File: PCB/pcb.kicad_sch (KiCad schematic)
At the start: 19 parts, among them J2 Conn_01x04, Q1 2N7002, SW1 SW_Push, U1 AT90USB1286-AU, Y1 Crystal_GND24_Small

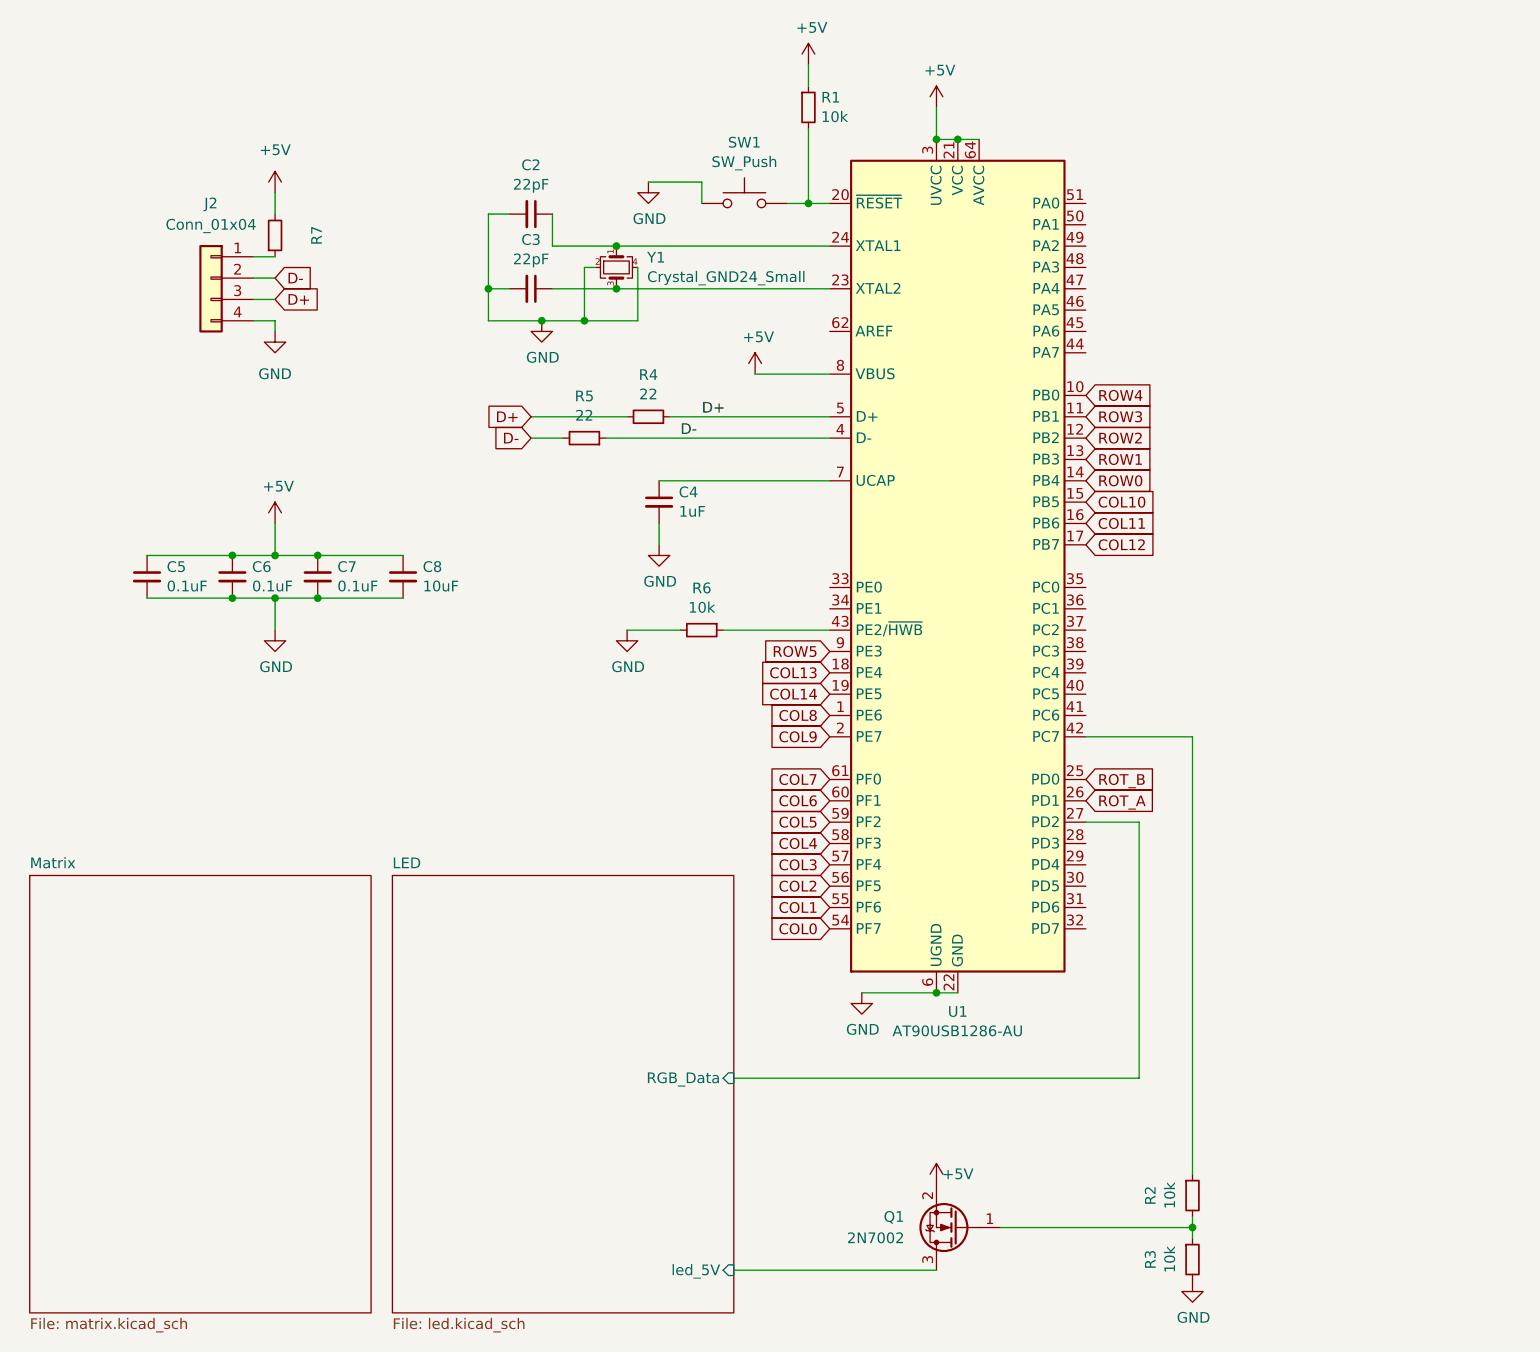
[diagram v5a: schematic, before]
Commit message: changes:\n\n -change zones\n -add mounting holes\n -change via size
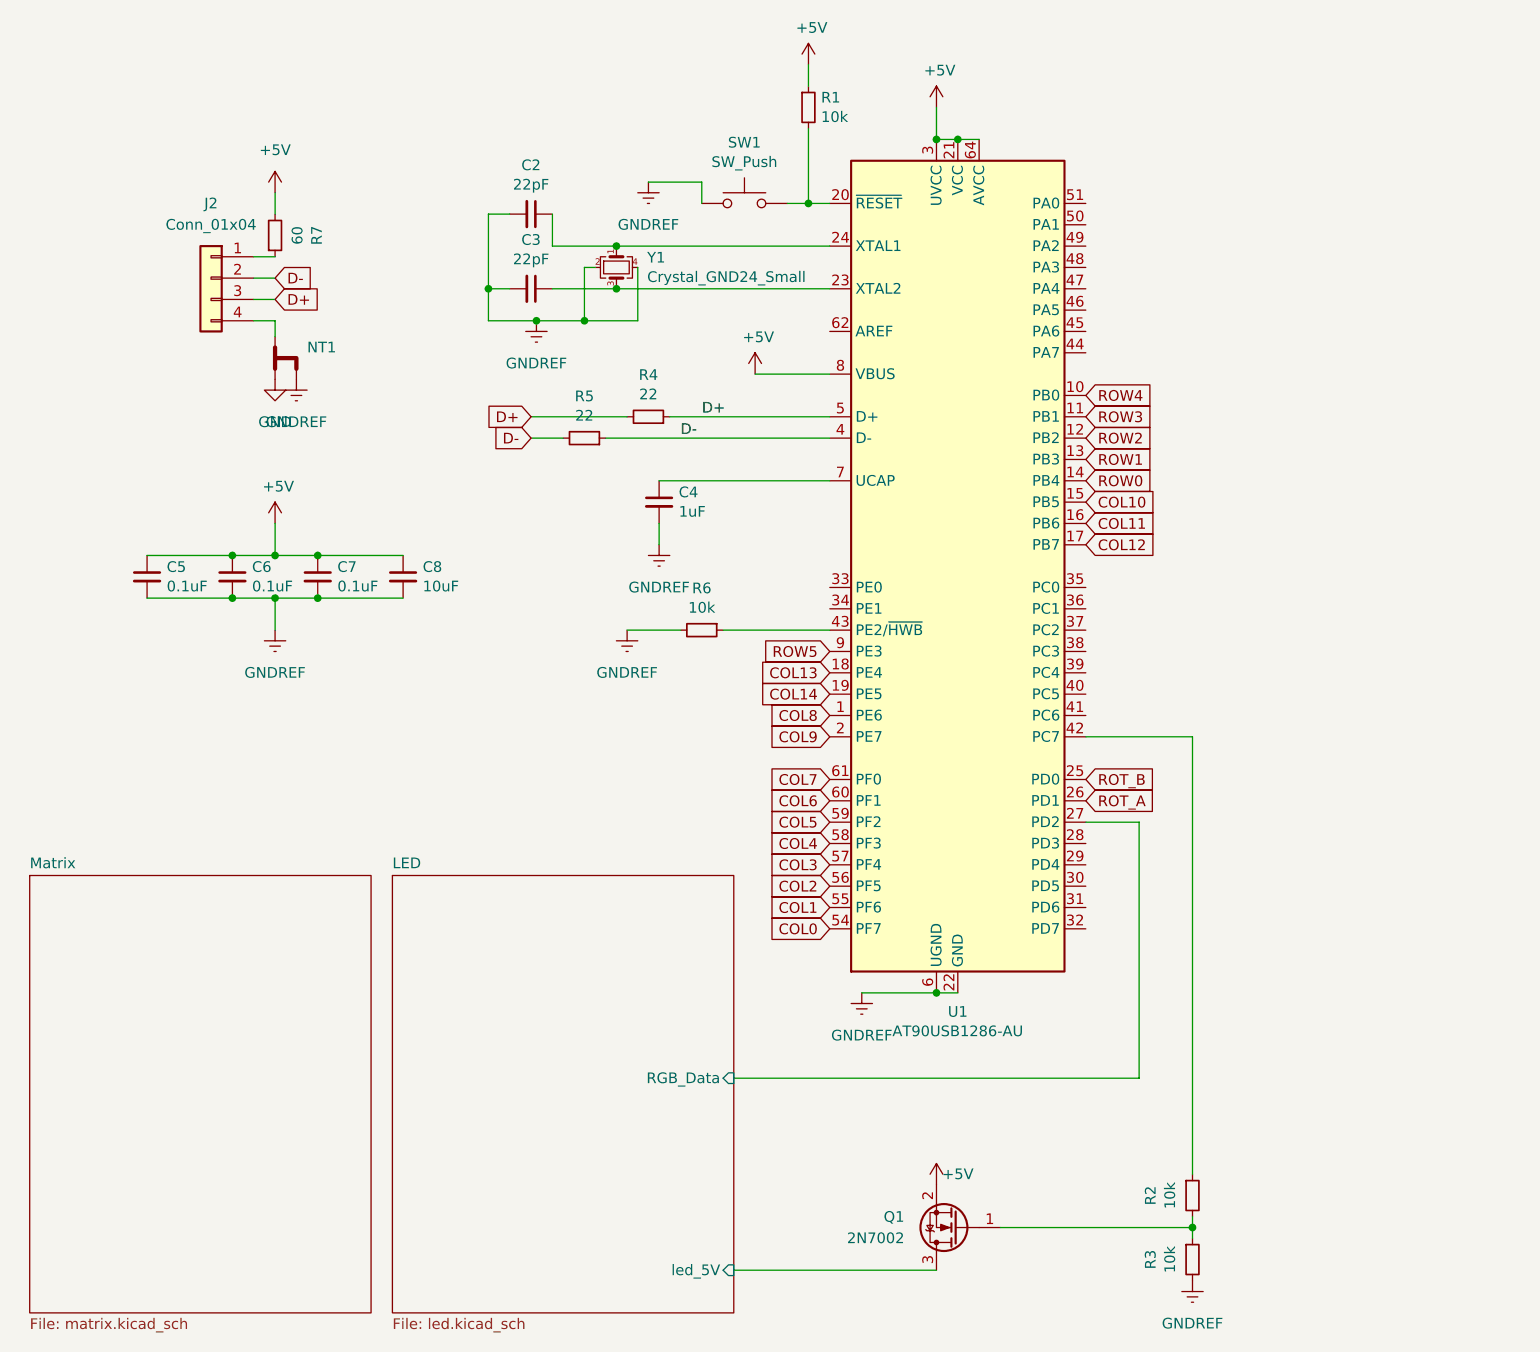
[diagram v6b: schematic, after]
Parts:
- added NT1: (no value), symbol Device:NetTie_3
- R7: value (none) -> 60; footprint (none) -> Resistor_SMD:R_0805_2012Metric
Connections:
- net GND: now also NT1.1; no longer C2.2, C3.2, C4.2, C5.2, C6.2, C7.2, C8.2, J2.4 (Pin_4), R3.2, R6.2, SW1.1, U1.22 (GND), U1.53 (GND), U1.6 (UGND), U1.63 (GND), Y1.2, Y1.4
- new net: J2.4 (Pin_4), NT1.2
- new net GNDREF: C2.2, C3.2, C4.2, C5.2, C6.2, C7.2, C8.2, NT1.3, R3.2, R6.2, SW1.1, U1.22 (GND), U1.53 (GND), U1.6 (UGND), U1.63 (GND), Y1.2, Y1.4

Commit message: production and CAD preparations
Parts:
- NT1: value (none) -> NetTie_3; footprint (none) -> NetTie:NetTie-3_SMD_Pad2.0mm
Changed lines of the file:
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@@
       (effects (font (size 1.27 1.27)) (justify right))
     )
-    (property "Value" "" (id 1) (at 49.53 57.7849 90)
+    (property "Value" "NetTie_3" (id 1) (at 49.53 57.7849 90)
       (effects (font (size 1.27 1.27)) (justify right))
     )
-    (property "Footprint" "" (id 2) (at 45.72 56.515 0)
+    (property "Footprint" "NetTie:NetTie-3_SMD_Pad2.0mm" (id 2) (at 45.72 56.515 0)
       (effects (font (size 1.27 1.27)) hide)
     )

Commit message: production?
still hope
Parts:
- added R9: (no value), symbol Device:R_Small
- C2: LCSC Part (none) -> C376875
- C3: value 22pF -> 0.1uF; LCSC Part (none) -> C38141
- C4: LCSC Part (none) -> C713511
- C5, C6: LCSC Part (none) -> C38141
- C7: value 0.1uF -> 22pF; LCSC Part (none) -> C376875
- C8: LCSC Part (none) -> C307525
- Q1: LCSC Part (none) -> C916396
- R1, R2, R3, R6: LCSC Part (none) -> C2907219
- R4, R5: LCSC Part (none) -> C2933536
- Y1: LCSC Part (none) -> C293959
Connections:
- net +5V: now also C3.1; no longer C7.1, Q1.2 (S)
- net GNDREF: now also R3.1, R6.1; no longer R3.2, R6.2
- net at U1.23 (XTAL2), Y1.3: now also C7.1; no longer C3.1
- net COL15: now reaches U1.35 (PC0)
- net COL16: now reaches U1.36 (PC1)
- net COL17: now reaches U1.37 (PC2)
- net at U1.42 (PC7): now also R2.2; no longer R2.1
- net at U1.43 (PE2/~{HWB}): now also R6.2; no longer R6.1
- net Power: now reaches J2.1 (Pin_1), R7.1
- net Power: now also R9.2
- new net: Q1.1 (G), R2.1, R3.2
- new net: Q1.2 (S), R9.1
